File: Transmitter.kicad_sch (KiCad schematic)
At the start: 12 parts, among them J1 Conn_01x02_Socket

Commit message: Added PCB v1
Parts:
- added C10: C, Capacitor_THT:C_Radial_D8.0mm_H11.5mm_P3.50mm, symbol Device:C
- C1, C2, C3: footprint (none) -> Capacitor_THT:C_Radial_D8.0mm_H11.5mm_P3.50mm
- R1, R2, R3, R4, R5: footprint (none) -> Resistor_THT:R_Axial_DIN0309_L9.0mm_D3.2mm_P12.70mm_Horizontal
- SignalSource1: renamed from SignalSource; footprint (none) -> Connector_PinHeader_2.54mm:PinHeader_1x02_P2.54mm_Vertical
- TransmitCoil1: renamed from TransmitCoil; footprint (none) -> Connector_PinHeader_2.54mm:PinHeader_1x02_P2.54mm_Vertical
- U1: footprint (none) -> Package_DIP:DIP-8_W7.62mm_Socket_LongPads
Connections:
- net GND1: now also C10.2
- net VCC: now also C10.1
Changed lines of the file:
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@@
+	)
+	(junction
+		(at 44.45 43.18)
+		(diameter 0)
+		(color 0 0 0 0)
 	)
 	(junction
@@
 	)
 	(junction
+		(at 44.45 50.8)
+		(diameter 0)
+		(color 0 0 0 0)
+	)
+	(junction
 		(at 114.3 105.41)
 		(diameter 0)
@@
 	(wire
 		(pts
-			(xy 44.45 39.37) (xy 44.45 45.72)
+			(xy 44.45 39.37) (xy 44.45 43.18)
 		)
 		(stroke
@@
 	(wire
 		(pts
+			(xy 44.45 43.18) (xy 48.26 43.18)
+		)
+		(stroke
+			(width 0)
+			(type default)
+		)
+	)
+	(wire
+		(pts
 			(xy 165.1 152.4) (xy 165.1 149.86)
 		)
@@
 	(wire
 		(pts
+			(xy 44.45 43.18) (xy 44.45 45.72)
+		)
+		(stroke
+			(width 0)
+			(type default)
+		)
+	)
+	(wire
+		(pts
 			(xy 101.6 88.9) (xy 101.6 86.36)
 		)
@@
 	(wire
 		(pts
-			(xy 44.45 48.26) (xy 44.45 53.34)
+			(xy 44.45 48.26) (xy 44.45 50.8)
 		)
 		(stroke
@@
 	(wire
 		(pts
+			(xy 48.26 50.8) (xy 44.45 50.8)
+		)
+		(stroke
+			(width 0)
+			(type default)
+		)
+	)
+	(wire
+		(pts
 			(xy 199.39 113.03) (xy 205.74 113.03)
 		)
@@
 		(pts
 			(xy 114.3 120.65) (xy 114.3 115.57)
+		)
+		(stroke
+			(width 0)
+			(type default)
+		)
+	)
+	(wire
+		(pts
+			(xy 44.45 50.8) (xy 44.45 53.34)
 		)
 		(stroke
@@
 		(dnp no)
 		(fields_autoplaced yes)
-		(property "Reference" "TransmitCoil"
+		(property "Reference" "TransmitCoil1"
 			(at 212.09 113.0299 0)
 			(effects
@@
 			)
 		)
-		(property "Footprint" ""
+		(property "Footprint" "Connector_PinHeader_2.54mm:PinHeader_1x02_P2.54mm_Vertical"
 			(at 210.82 113.03 0)
 			(effects
@@
 			(project "AmplifierCircuit"
 				(path "/1187d58b-5bff-4ac8-89f7-59cd1d310934/5958d90b-b390-4fdf-a917-7468261062da"
-					(reference "TransmitCoil")
+					(reference "TransmitCoil1")
 					(unit 1)
 				)
@@
 			)
 		)
-		(property "Footprint" ""
+		(property "Footprint" "Resistor_THT:R_Axial_DIN0309_L9.0mm_D3.2mm_P12.70mm_Horizontal"
 			(at 163.322 133.35 90)
 			(effects
@@
 			)
 		)
-		(property "Footprint" ""
+		(property "Footprint" "Capacitor_THT:C_Radial_D8.0mm_H11.5mm_P3.50mm"
 			(at 166.0652 149.86 0)
 			(effects
@@
 			)
 		)
-		(property "Footprint" ""
+		(property "Footprint" "Capacitor_THT:C_Radial_D8.0mm_H11.5mm_P3.50mm"
 			(at 91.1352 73.66 0)
 			(effects
@@
 			)
 		)
-		(property "Footprint" ""
+		(property "Footprint" "Resistor_THT:R_Axial_DIN0309_L9.0mm_D3.2mm_P12.70mm_Horizontal"
 			(at 112.522 69.85 90)
 			(effects
@@
 		(dnp no)
 		(fields_autoplaced yes)
-		(property "Reference" "SignalSource"
+		(property "Reference" "SignalSource1"
 			(at 102.235 115.57 0)
 			(effects
@@
 			)
 		)
-		(property "Footprint" ""
+		(property "Footprint" "Connector_PinHeader_2.54mm:PinHeader_1x02_P2.54mm_Vertical"
 			(at 101.6 123.19 0)
 			(effects
@@
 			(project ""
 				(path "/1187d58b-5bff-4ac8-89f7-59cd1d310934/5958d90b-b390-4fdf-a917-7468261062da"
-					(reference "SignalSource")
+					(reference "SignalSource1")
 					(unit 1)
 				)
@@
 	)
 	(symbol
+		(lib_id "Device:C")
+		(at 48.26 46.99 0)
+		(unit 1)
+		(exclude_from_sim no)
+		(in_bom yes)
+		(on_board yes)
+		(dnp no)
+		(fields_autoplaced yes)
+		(property "Reference" "C10"
+			(at 52.07 45.7199 0)
+			(effects
+				(font
+					(size 1.27 1.27)
+				)
+				(justify left)
+			)
+		)
+		(property "Value" "C"
+			(at 52.07 48.2599 0)
+			(effects
+				(font
+					(size 1.27 1.27)
+				)
+				(justify left)
+			)
+		)
+		(property "Footprint" "Capacitor_THT:C_Radial_D8.0mm_H11.5mm_P3.50mm"
+			(at 49.2252 50.8 0)
+			(effects
+				(font
+					(size 1.27 1.27)
+				)
+				(hide yes)
+			)
+		)
+		(property "Datasheet" "~"
+			(at 48.26 46.99 0)
+			(effects
+				(font
+					(size 1.27 1.27)
+				)
+				(hide yes)
+			)
+		)
+		(property "Description" "Unpolarized capacitor"
+			(at 48.26 46.99 0)
+			(effects
+				(font
+					(size 1.27 1.27)
+				)
+				(hide yes)
+			)
+		)
+		(pin "1"
+		)
+		(pin "2"
+		)
+		(instances
+			(project "AmplifierCircuit"
+				(path "/1187d58b-5bff-4ac8-89f7-59cd1d310934/5958d90b-b390-4fdf-a917-7468261062da"
+					(reference "C10")
+					(unit 1)
+				)
+			)
+		)
+	)
+	(symbol
 		(lib_id "Device:R")
 		(at 176.53 114.3 0)
@@
 			)
 		)
-		(property "Footprint" ""
+		(property "Footprint" "Resistor_THT:R_Axial_DIN0309_L9.0mm_D3.2mm_P12.70mm_Horizontal"
 			(at 174.752 114.3 90)
 			(effects
@@
 			)
 		)
-		(property "Footprint" ""
+		(property "Footprint" "Resistor_THT:R_Axial_DIN0309_L9.0mm_D3.2mm_P12.70mm_Horizontal"
 			(at 99.822 69.85 90)
 			(effects
@@
 			)
 		)
-		(property "Footprint" ""
+		(property "Footprint" "Capacitor_THT:C_Radial_D8.0mm_H11.5mm_P3.50mm"
 			(at 115.2652 115.57 0)
 			(effects
@@
 			)
 		)
-		(property "Footprint" ""
+		(property "Footprint" "Package_DIP:DIP-8_W7.62mm_Socket_LongPads"
 			(at 154.94 107.95 0)
 			(effects
@@
 			)
 		)
-		(property "Footprint" ""
+		(property "Footprint" "Package_DIP:DIP-8_W7.62mm_Socket_LongPads"
 			(at 60.96 46.99 0)
 			(effects
@@
 			)
 		)
-		(property "Footprint" ""
+		(property "Footprint" "Resistor_THT:R_Axial_DIN0309_L9.0mm_D3.2mm_P12.70mm_Horizontal"
 			(at 99.822 82.55 90)
 			(effects

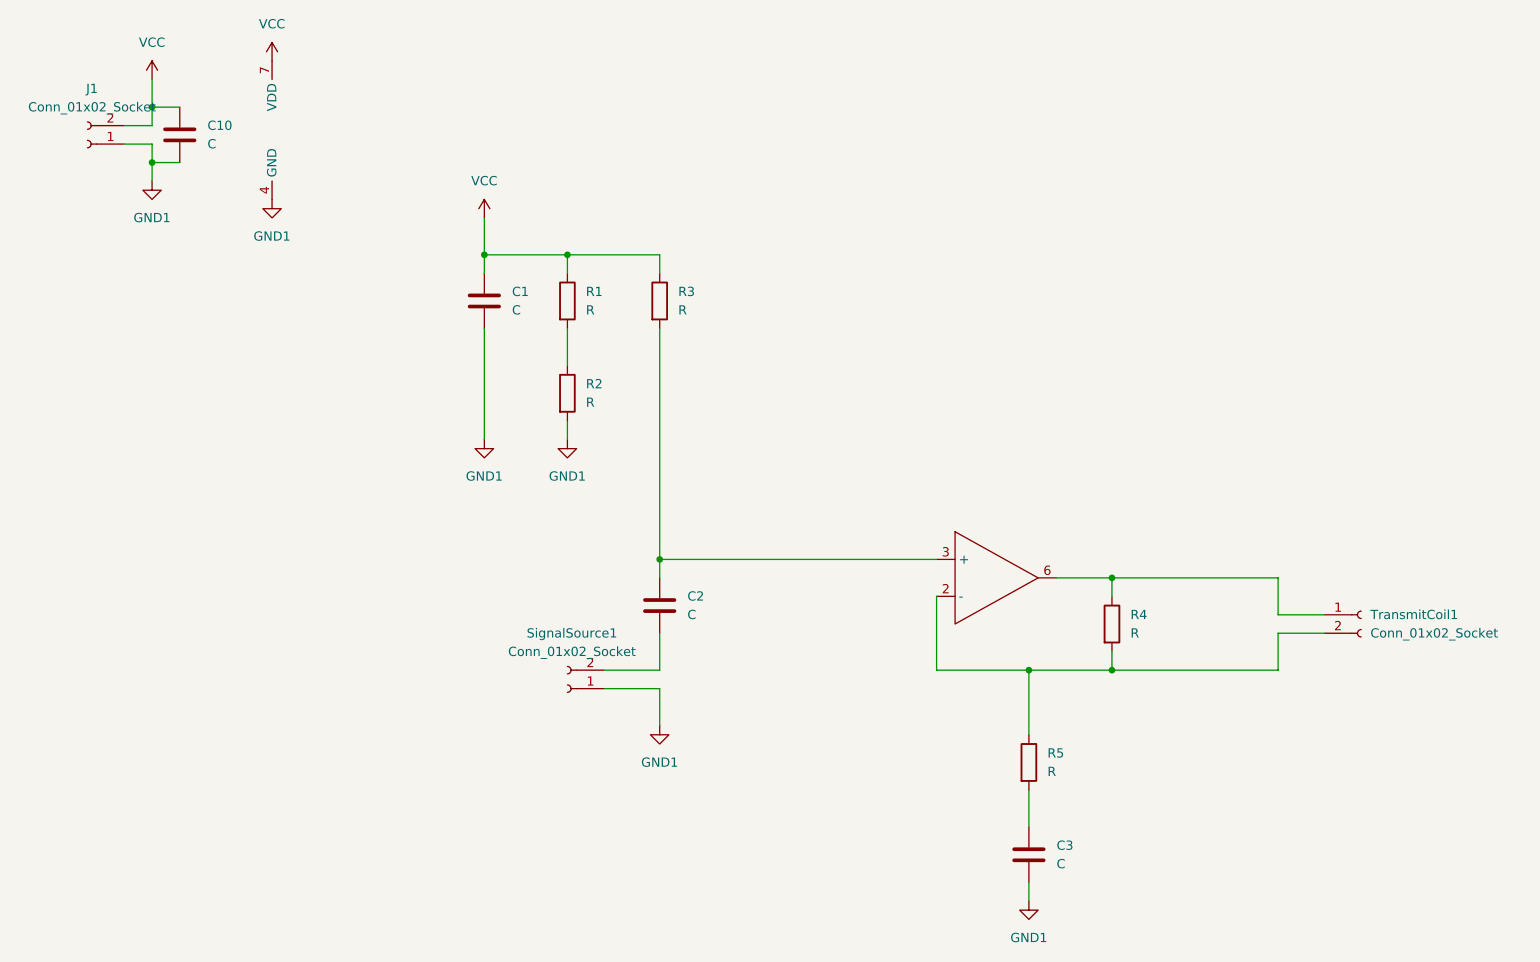
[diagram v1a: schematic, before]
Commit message: Updated the footprints for SMD
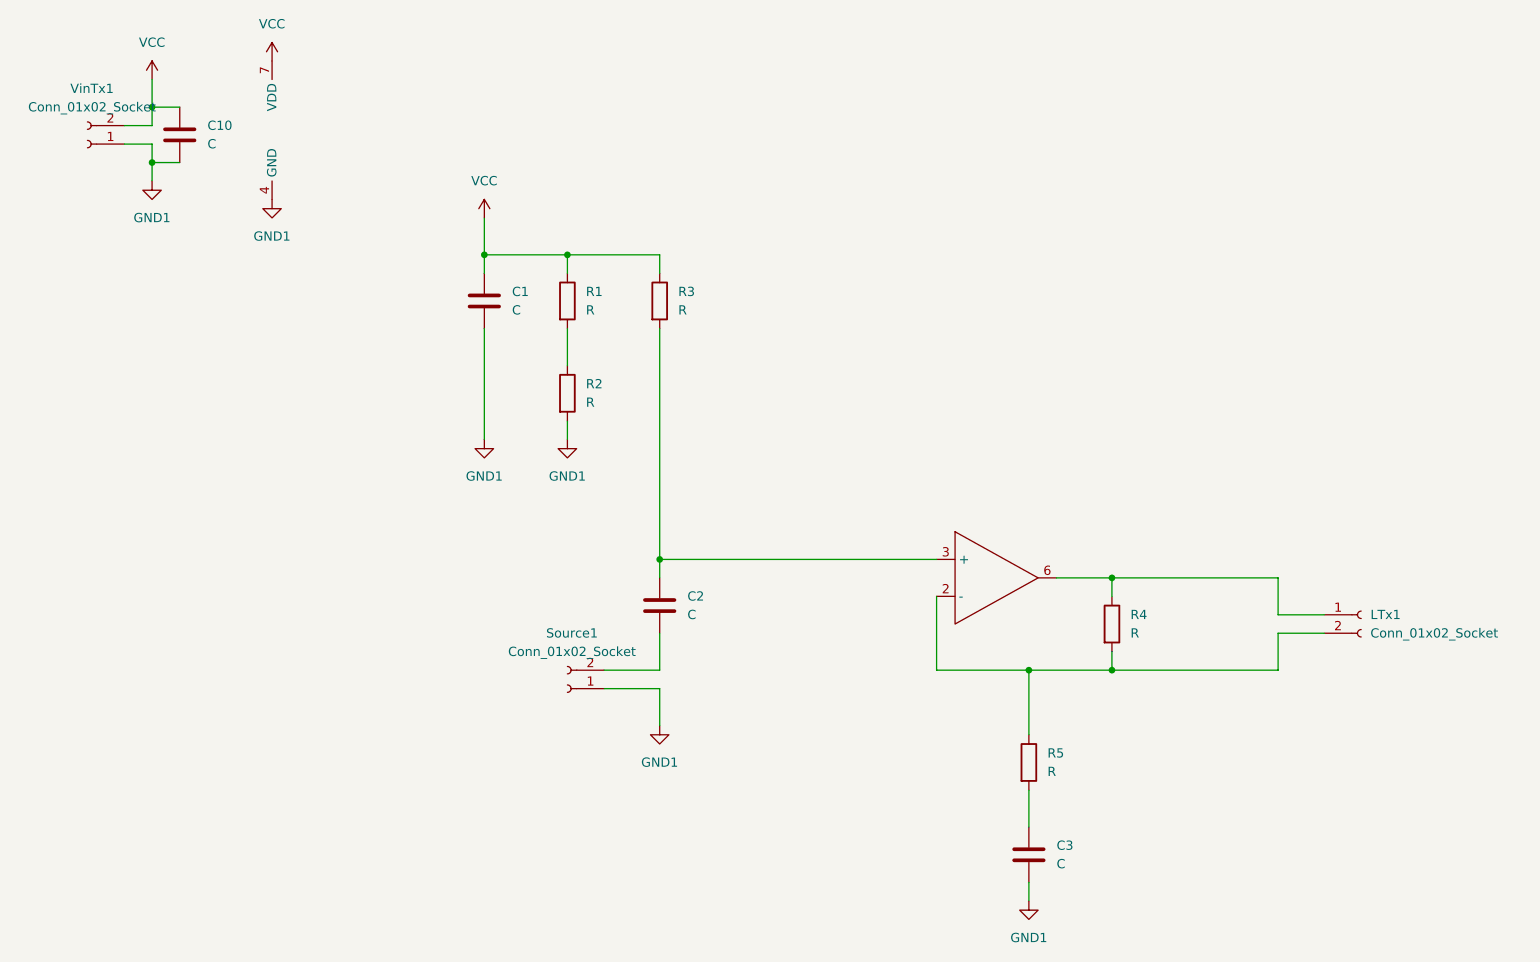
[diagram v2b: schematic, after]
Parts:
- U1: footprint Package_DIP:DIP-8_W7.62mm_Socket_LongPads -> Package_SO:SOIC-8_5.3x5.3mm_P1.27mm
- renumbered TransmitCoil1 to LTx1, SignalSource1 to Source1, J1 to VinTx1
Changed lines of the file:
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@@
 		(dnp no)
 		(fields_autoplaced yes)
-		(property "Reference" "TransmitCoil1"
+		(property "Reference" "LTx1"
 			(at 212.09 113.0299 0)
 			(effects
@@
 			(project "AmplifierCircuit"
 				(path "/1187d58b-5bff-4ac8-89f7-59cd1d310934/5958d90b-b390-4fdf-a917-7468261062da"
-					(reference "TransmitCoil1")
+					(reference "LTx1")
 					(unit 1)
 				)
@@
 		(dnp no)
 		(fields_autoplaced yes)
-		(property "Reference" "J1"
+		(property "Reference" "VinTx1"
 			(at 36.195 40.64 0)
 			(effects
@@
 			(project ""
 				(path "/1187d58b-5bff-4ac8-89f7-59cd1d310934/5958d90b-b390-4fdf-a917-7468261062da"
-					(reference "J1")
+					(reference "VinTx1")
 					(unit 1)
 				)
@@
 		(dnp no)
 		(fields_autoplaced yes)
-		(property "Reference" "SignalSource1"
+		(property "Reference" "Source1"
 			(at 102.235 115.57 0)
 			(effects
@@
 			(project ""
 				(path "/1187d58b-5bff-4ac8-89f7-59cd1d310934/5958d90b-b390-4fdf-a917-7468261062da"
-					(reference "SignalSource1")
+					(reference "Source1")
 					(unit 1)
 				)
@@
 			)
 		)
-		(property "Footprint" "Package_DIP:DIP-8_W7.62mm_Socket_LongPads"
+		(property "Footprint" "Package_SO:SOIC-8_5.3x5.3mm_P1.27mm"
 			(at 154.94 107.95 0)
 			(effects
@@
 			)
 		)
-		(property "Footprint" "Package_DIP:DIP-8_W7.62mm_Socket_LongPads"
+		(property "Footprint" "Package_SO:SOIC-8_5.3x5.3mm_P1.27mm"
 			(at 60.96 46.99 0)
 			(effects
